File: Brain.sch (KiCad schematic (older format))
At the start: 5 parts, among them J1 Conn_01x04_Male, U2 AT24C32

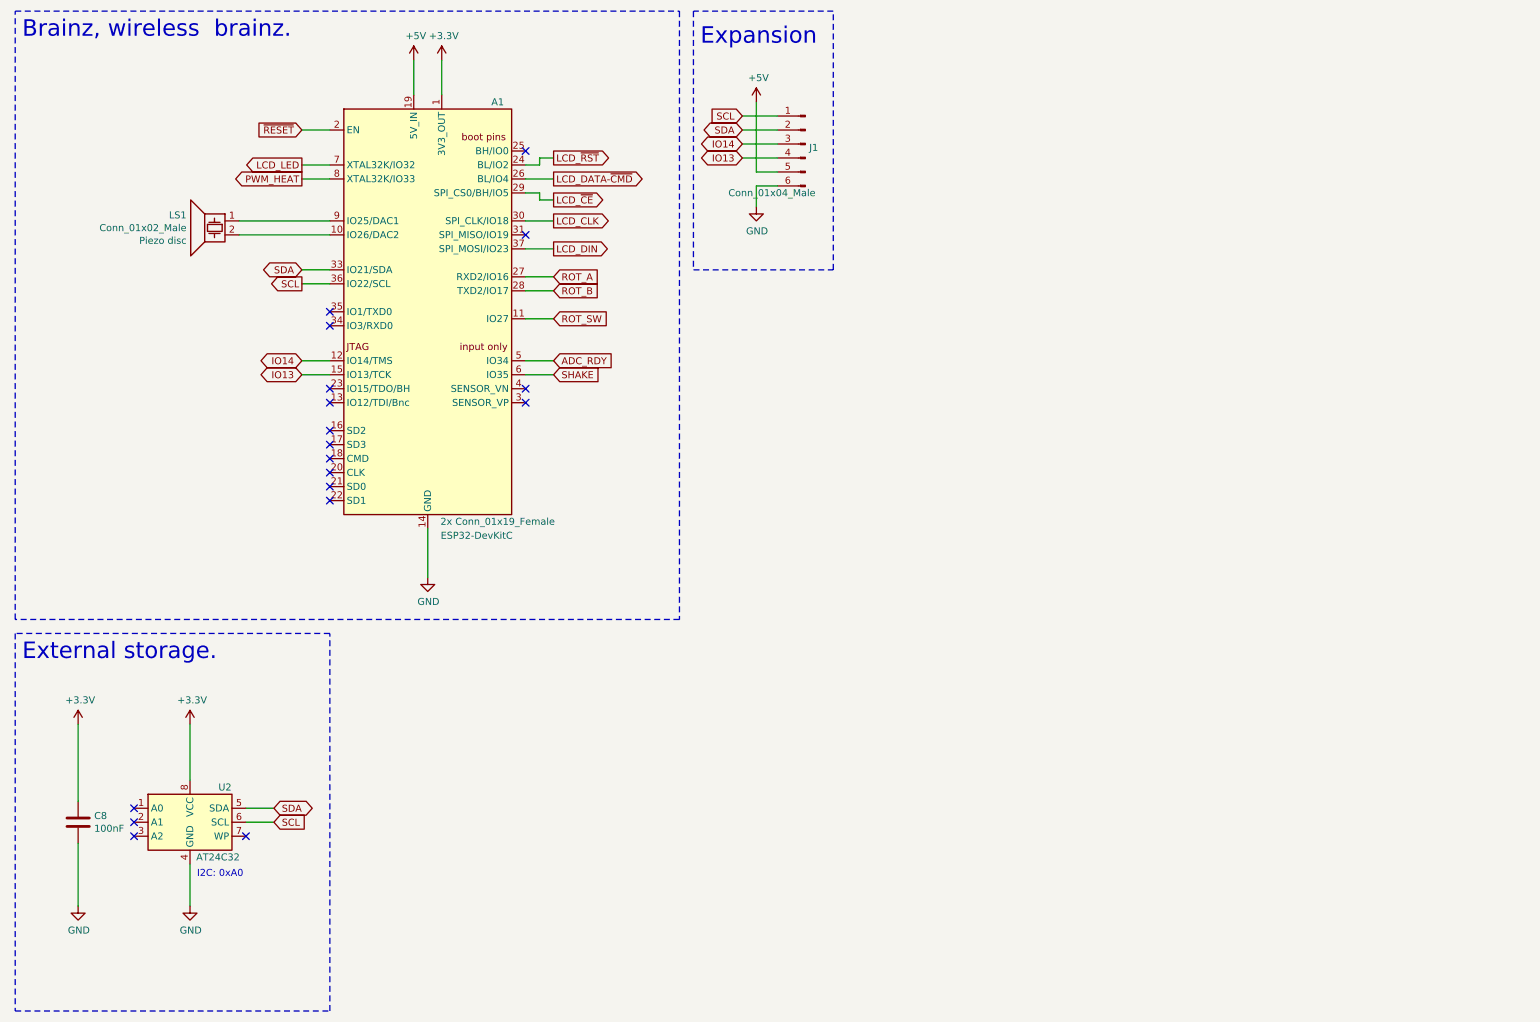
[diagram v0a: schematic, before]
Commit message: Added overheat protection that works, but very noisy.
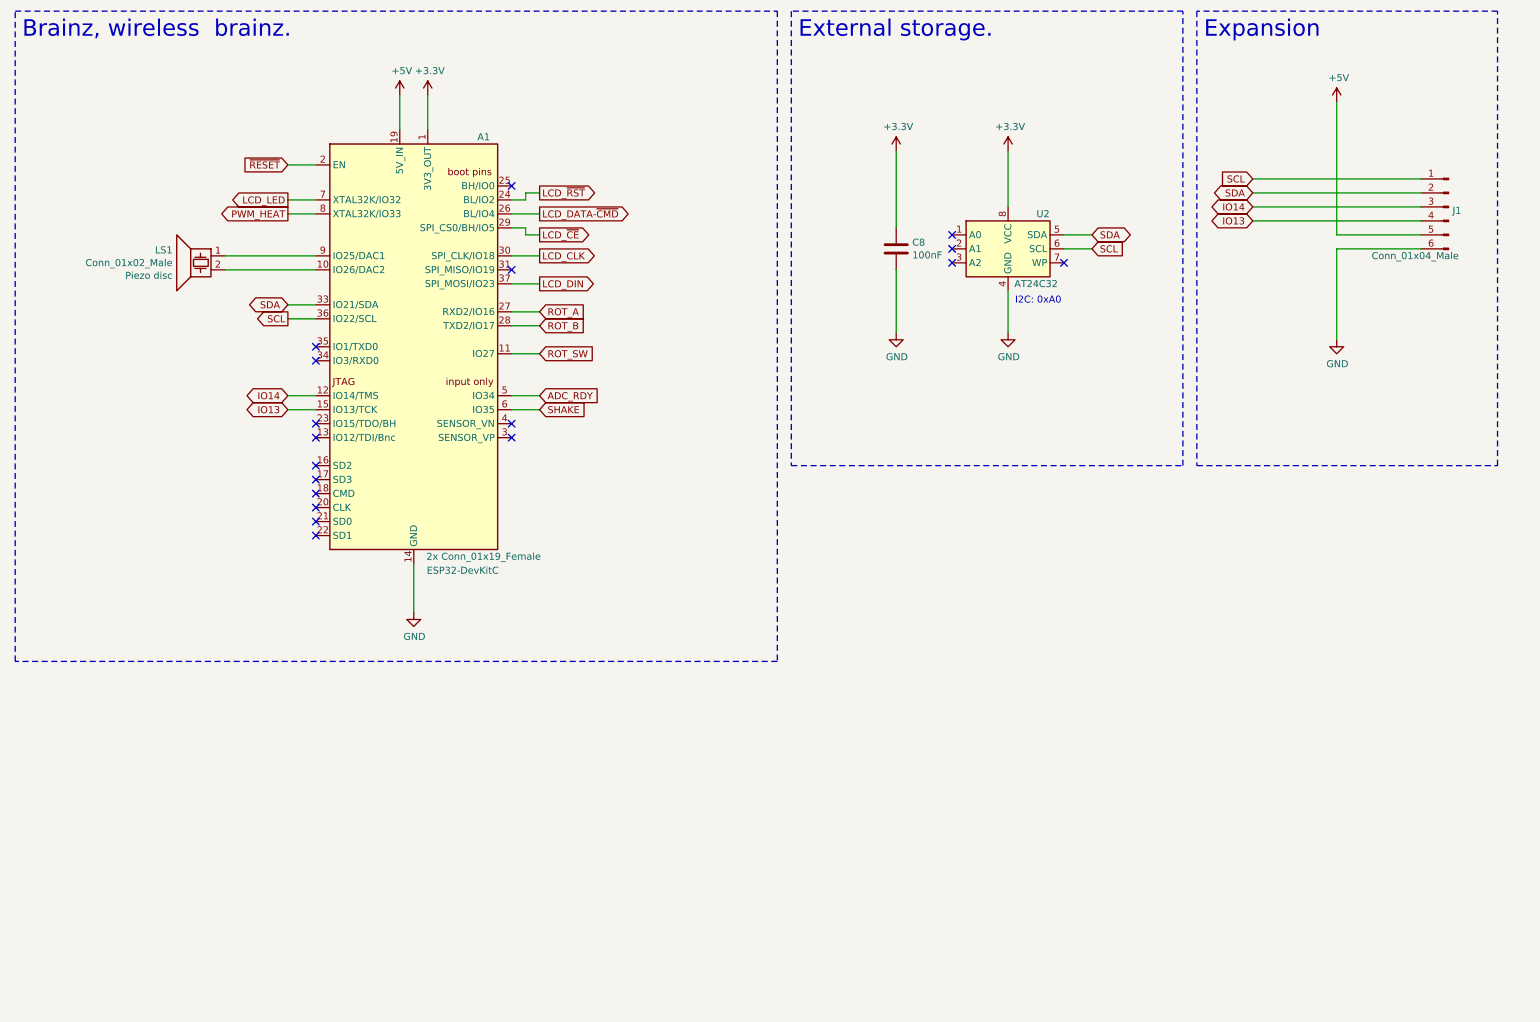
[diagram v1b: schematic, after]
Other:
- moved on the sheet: A1, C8, J1, LS1, U2

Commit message: V2.0 pcb.
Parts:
- removed C8: 100nF, Capacitor_SMD:C_0805_2012Metric_Pad1.18x1.45mm_HandSolder, symbol Device:C
- removed J1: Conn_01x04_Male, Connector_PinHeader_2.54mm:PinHeader_1x06_P2.54mm_Vertical, symbol Connector:Conn_01x06_Male
- removed LS1: Conn_01x02_Male, Connector_PinHeader_2.54mm:PinHeader_1x02_P2.54mm_Vertical, symbol Device:Speaker_Crystal
- removed U2: AT24C32, Package_SO:SO-8_3.9x4.9mm_P1.27mm, symbol Memory_EEPROM:24LC32
- added C1, C2: 6.7pF, Capacitor_SMD:C_0805_2012Metric_Pad1.18x1.45mm_HandSolder, symbol Device:C
- added C35, C36, C37, C38: 100nF, Capacitor_SMD:C_0805_2012Metric_Pad1.18x1.45mm_HandSolder, symbol Device:C
- added C40, C41: 1uF, Capacitor_SMD:C_0805_2012Metric_Pad1.18x1.45mm_HandSolder, symbol Device:C
- added C50: 4.7uF, Capacitor_SMD:C_0805_2012Metric_Pad1.18x1.45mm_HandSolder, symbol Device:C
- added C60, C61: 10uF, Capacitor_SMD:C_0805_2012Metric_Pad1.18x1.45mm_HandSolder, symbol Device:C
- added C72, C73: 100uF/35V, Capacitor_SMD:CP_Elec_6.3x7.7, symbol Device:CP
- added D10: Amber, LED_SMD:LED_0805_2012Metric_Pad1.15x1.40mm_HandSolder, symbol Device:LED
- added D3, D4: BAV99, Package_TO_SOT_SMD:SOT-23, symbol Diode:BAV99
- added J10: USB_B_Micro, Connector_USB:USB_Micro-B_Amphenol_10118194_Horizontal, symbol Connector:USB_B_Micro
- added J11: Conn_ARM_JTAG_SWD_10, Connector_PinHeader_2.54mm:PinHeader_2x05_P2.54mm_Vertical, symbol Connector:Conn_ARM_JTAG_SWD_10
- added L2: 10uH, Inductor_SMD:L_0805_2012Metric_Pad1.15x1.40mm_HandSolder, symbol Device:L_Small
- added NT2: ~, NetTie-extra:NetTie-2_SMD_Pad0.25mm, symbol Device:Net-Tie_2
- added R20: 470R, Resistor_SMD:R_0805_2012Metric_Pad1.20x1.40mm_HandSolder, symbol Device:R
- added R53, R54, R55, R56, R57: 4k7, Resistor_SMD:R_0805_2012Metric_Pad1.20x1.40mm_HandSolder, symbol Device:R
- added SW2: SW_Push, Button_Switch_SMD:SW_SPST_CK_RS282G05A3, symbol Switch:SW_Push
- added U1: ATSAMD21G, Package_QFP:TQFP-48_7x7mm_P0.5mm, symbol MCU_Microchip_SAMD-extra:SAMD21G_ARDUINO_M0
- added Y1: 32768Hz, Crystal:Crystal_C26-LF_D2.1mm_L6.5mm_Horizontal_1EP_style1, symbol Device:Crystal_GND3
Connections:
- net +3V3: now also C36.1, C40.1, C60.1, C73.1, D3.2 (A), D4.2 (A), J11.1 (VTref), L2.2, R53.2, R54.2, R55.2, R56.2, U1.17 (VDDIO), U1.36 (VDDIO), U1.44 (VDDIN)
- net +5V: now also C72.1
- net ADC_RDY: now also U1.11 (PA06/~~D8); no longer A1.5 (IO34)
- net GND: now also C1.2, C2.2, C35.2, C36.2, C37.2, C38.2, C40.2, C41.2, C50.2, C60.2, C61.2, C72.2, C73.2, D10.1 (K), D3.1 (K), D4.1 (K), J11.3 (GND), J11.5 (GND), J11.9 (GNDDetect), NT2.2, SW2.1, U1.18 (GND), U1.35 (GND), U1.42 (GND), U1.5 (GNDANA)
- net PWM_HEAT: now also U1.25 (PA16/~~D11); no longer A1.8 (XTAL32K/IO33)
- net ROT_SW: now also A1.8 (XTAL32K/IO33); no longer A1.11 (IO27)
- net I2S_WS: now reaches A1.10 (IO26/DAC2)
- net ESP32_IO0: now reaches A1.25 (BH/IO0)
- net ESP32_IO0: now also U1.28 (PA19/~~D12)
- net ESP32_RXD: now reaches A1.34 (IO3/RXD0)
- net ESP32_RXD: now also U1.15 (PA10/D1/TX)
- net ESP32_TXD: now reaches A1.35 (IO1/TXD0)
- net ESP32_TXD: now also U1.16 (PA11/D0/RX)
- net I2S_BCK: now reaches A1.9 (IO25/DAC1)
- net IO13: no longer names the net of A1.15 (IO13/TCK)
- net IO14 renamed HEAT_INT
- net HEAT_INT: now also U1.23 (PA14/D2)
- net SCL renamed ESP32_SCL
- net ESP32_SCL: now also R55.1, U1.13 (PA08/~~D4)
- net SDA renamed ESP32_SDA
- net ESP32_SDA: now also R56.1, U1.14 (PA09/~~D3)
- net SHAKE: no longer names the net of A1.6 (IO35)
- net ~RESET renamed ESP32_EN
- net ESP32_EN: now also U1.27 (PA18/~~D10)
- new net: J10.5 (GND), J10.6 (Shield), NT2.1
- new net: R20.1, SW2.2
- new net: D10.2 (A), R57.1
- new net +3.3VA: C35.1, C61.1, L2.1, U1.6 (VDDANA)
- new net AIN_COMP: U1.8 (PB09/A2), U1.9 (PA04/A3)
- new net AREF: C37.1, C50.1, U1.4 (PA03/AREF)
- new net DEBUG_LED: R57.2, U1.26 (PA17/~~D13/LED)
- new net HEAT_SCL: R54.1, U1.31 (PA22/SDA)
- new net HEAT_SDA: R53.1, U1.32 (PA23/SCL)
- new net HEAT_~RESET: C38.1, J11.10 (~RESET~), R20.2, U1.40 (RESET)
- new net I2S_DATA: A1.11 (IO27)
- new net I2S_GAIN0: U1.24 (PA15/~~D5)
- new net I2S_GAIN1: U1.29 (PA20/~~D6)
- new net I2S_SD: U1.30 (PA21/D7)
- new net IRON_POWER: U1.47 (PB02/A5)
- new net NTC: U1.3 (PA02/DAC/A0)
- new net SWCLK: J11.4 (SWDCLK/TCK), U1.45 (PA30/SWCLK)
- new net SWDIO: J11.2 (SWDIO/TMS), U1.46 (PA31/SWDIO)
- new net TEMP: U1.7 (PB08/A1)
- new net USB+: D3.3 (K), J10.3 (D+), U1.34 (PA25/USB+)
- new net USB-: D4.3 (K), J10.2 (D-), U1.33 (PA24/USB-)
- new net VDDCORE: C41.1, U1.43 (VDDCORE)
- new net VIN: U1.10 (PA05/A4)
- new net XIN32: C1.1, U1.1 (PA00/XIN32), Y1.1
- new net XOUT32: C2.1, U1.2 (PA01/XOUT32), Y1.2
- no-connect marks 18 -> 29
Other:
- note added: "Debug LED"
- note added: "ESP32 wireless module"
- note added: "Heat controller"
- note added: "Heat controller SWD"
- note added: "Heat controller reset"
- note added: "The pull is strong"
- note removed: "Brainz, wireless brainz."
- note removed: "Expansion"
- note removed: "External storage."
- note removed: "I2C: 0xA0"
- moved on the sheet: A1

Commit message: V2.0 pcb.
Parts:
- removed C72: 100uF/35V, Capacitor_SMD:CP_Elec_6.3x7.7, symbol Device:CP
- removed NT2: ~, NetTie-extra:NetTie-2_SMD_Pad0.25mm, symbol Device:Net-Tie_2
- added C22: 1nF, Capacitor_SMD:C_0805_2012Metric_Pad1.18x1.45mm_HandSolder, symbol Device:C
- added J9: Conn_ARM_JTAG_SWD_10, Connector_PinHeader_2.54mm:PinHeader_2x05_P2.54mm_Vertical, symbol Connector:Conn_ARM_JTAG_SWD_10
- added R84: 1M, Resistor_SMD:R_0805_2012Metric_Pad1.20x1.40mm_HandSolder, symbol Device:R
- added TP1, TP2, TP3, TP4: TestPoint, TestPoint-extra:TestPoint_Pad_D0.75mm, symbol Connector:TestPoint
- added U6: AT24C32, Package_SO:SO-8_3.9x4.9mm_P1.27mm, symbol Memory_EEPROM:24LC32
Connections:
- net +3V3: now also J9.1 (VTref), U6.8 (VCC)
- net GND: now also J10.5 (GND), C22.2, J9.3 (GND), J9.5 (GND), J9.9 (GNDDetect), R84.1, U6.4 (GND)
- net HEAT_INT: now also A1.6 (IO35); no longer A1.12 (IO14/TMS)
- net HEAT_SCL: now also U6.6 (SCL)
- net HEAT_SDA: now also U6.5 (SDA)
- net at A1.13 (IO12/TDI/Bnc): now also J9.8 (NC/TDI)
- net at A1.15 (IO13/TCK): now also J9.4 (SWDCLK/TCK)
- net at A1.23 (IO15/TDO/BH): now also J9.6 (SWO/TDO)
- net D9: now reaches U1.12 (PA07/~~D9)
- net D9: now also TP3.1
- net at J10.6 (Shield): now also C22.1, R84.2; no longer J10.5 (GND)
- net ESP32_EN renamed D10
- net D10: now also TP4.1; no longer A1.2 (EN)
- net ESP32_IO0: no longer names the net of A1.25 (BH/IO0)
- net ESP32_IO0: no longer U1.28 (PA19/~~D12)
- net ESP32_RXD: no longer names the net of A1.34 (IO3/RXD0)
- net ESP32_RXD: no longer U1.15 (PA10/D1/TX)
- net ESP32_TXD: no longer names the net of A1.35 (IO1/TXD0)
- net ESP32_TXD: no longer U1.16 (PA11/D0/RX)
- net IRON_POWER renamed IRON_CURRENT
- new net: A1.12 (IO14/TMS), J9.2 (SWDIO/TMS)
- new net D0: TP1.1, U1.16 (PA11/D0/RX)
- new net D1: TP2.1, U1.15 (PA10/D1/TX)
- new net EN: A1.2 (EN), J9.10 (~RESET~)
- no-connect marks 29 -> 32
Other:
- note added: "EEPROM"
- moved on the sheet: A1, C1, C2, C35, C36, C37, C38, C40, C41, C50, C60, C61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
